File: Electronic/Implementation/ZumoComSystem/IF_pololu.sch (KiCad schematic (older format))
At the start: 38 parts, among them J4 Left, J5 Conn_02x07_Odd_Even, J6 Right, J7 Conn_02x07_Odd_Even, Q10 SI2302CDS-T1-BE3, Q6 SI2302CDS-T1-BE3, Q7 SI2302CDS-T1-BE3, Q8 SI2302CDS-T1-BE3, Q9 SI2302CDS-T1-BE3, SW3 SW_Push, SW4 SW_Push, SW5 SW_Push

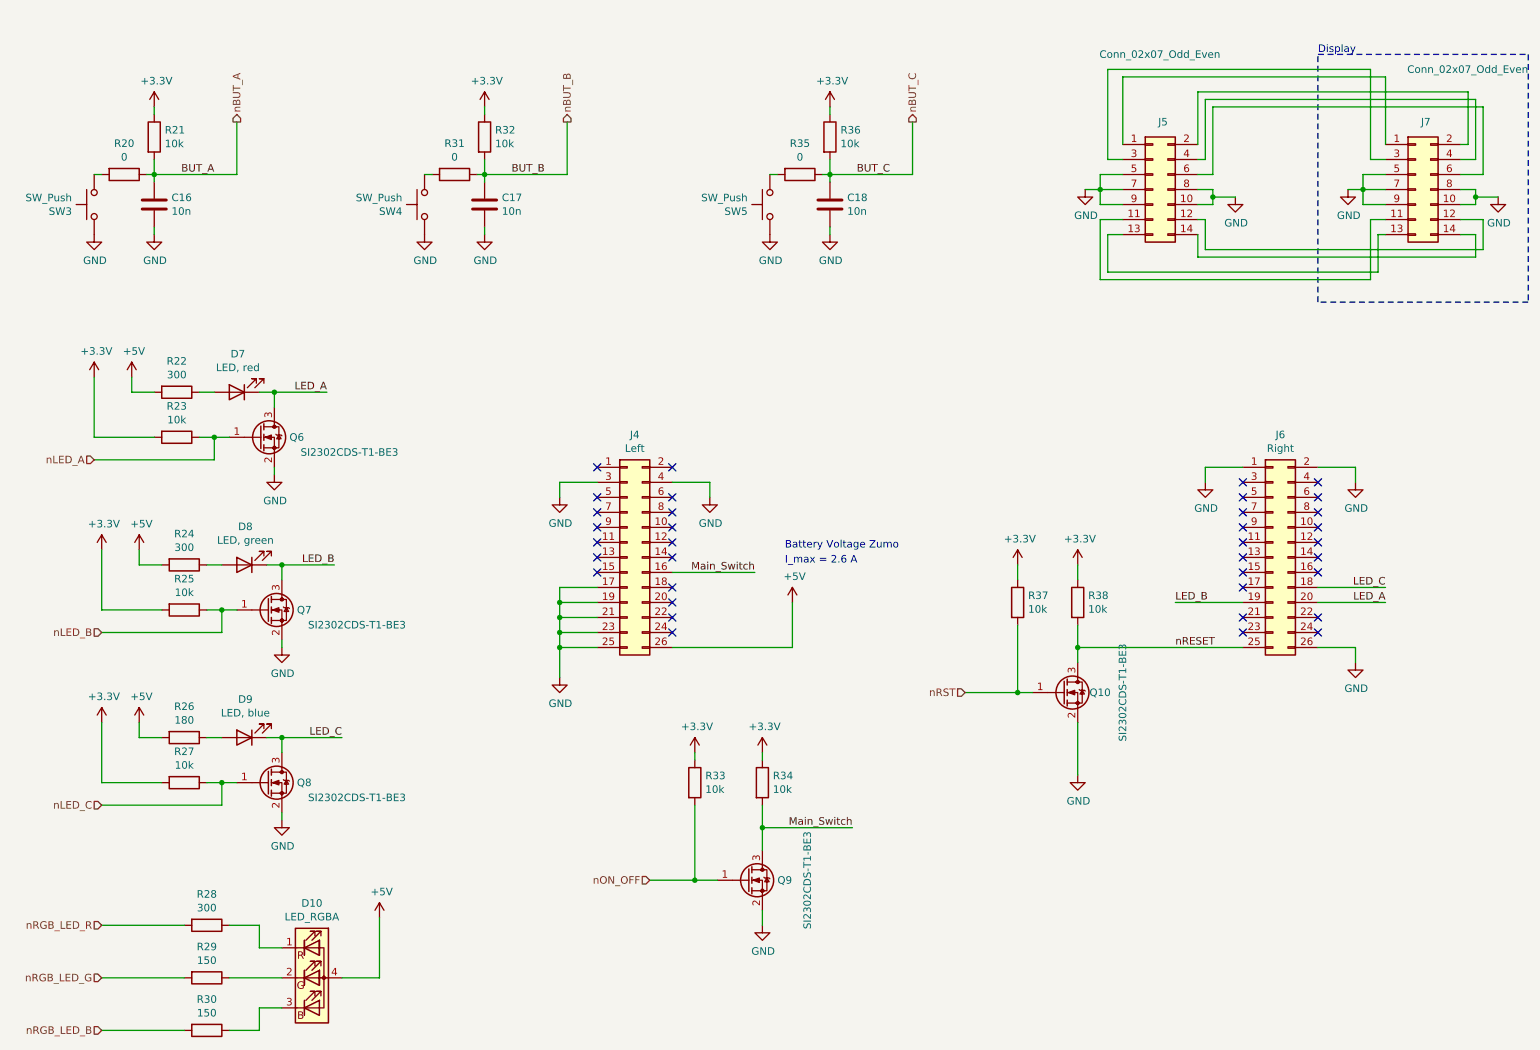
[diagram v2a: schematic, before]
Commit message: Electronic: ZumoCom System: finhished/ orderd PCB + add Version and TOP/BOT on PCB
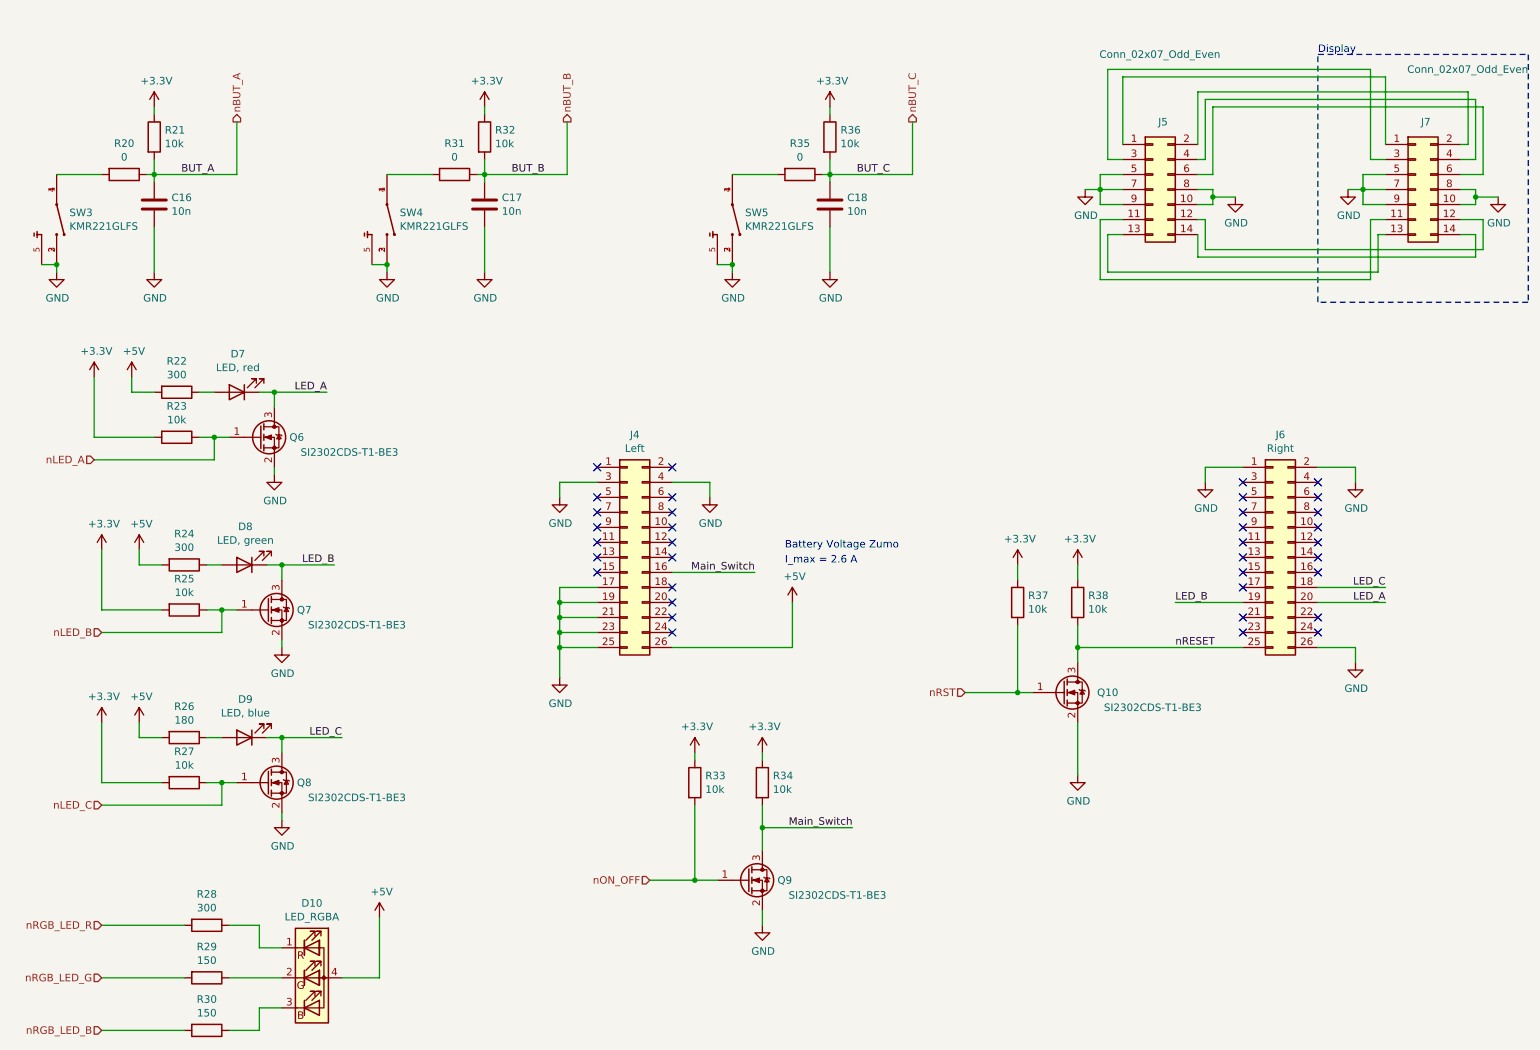
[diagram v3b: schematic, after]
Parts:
- removed SW3, SW4, SW5: SW_Push, Button_Switch_SMD:SW_SPST_B3U-1000P-B, symbol Switch:SW_Push
- added SW3, SW4, SW5: KMR221GLFS, footprints:SW_KMR221GLFS, symbol KMR221GLFS:KMR221GLFS
- R26: Part-No. RL73N1JR18JTD -> CRGP0603F180R
- R29, R30: Manufacturer Panasonic Electronic Components -> YAGEO; Part-No. ERJ-3RSFR15V -> RC0603FR-07150RL
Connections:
- net GND: now also SW3.2, SW3.3, SW3.5, SW4.2, SW4.3, SW4.5, SW5.2, SW5.3, SW5.5
- net at R31.2: now also SW4.1, SW4.4
- net at R35.2: now also SW5.1, SW5.4
- net at R20.2: now also SW3.1, SW3.4
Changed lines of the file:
@@
 Sheet 7 7
 Title "Zumo Communication System"
-Date "2022-04-22"
+Date "2022-05-13"
 Rev "V1.0"
 Comp "NewTec GmbH"
@@
 F 2 "Resistor_SMD:R_0603_1608Metric_Pad1.05x0.95mm_HandSolder" V 2030 6900 50  0001 C CNN
 F 3 "~" H 2100 6900 50  0001 C CNN
-F 4 "Panasonic Electronic Components" H 2100 6900 50  0001 C CNN "Manufacturer"
-F 5 "ERJ-3RSFR15V" H 2100 6900 50  0001 C CNN "Part-No."
+F 4 "YAGEO" H 2100 6900 50  0001 C CNN "Manufacturer"
+F 5 "RC0603FR-07150RL" H 2100 6900 50  0001 C CNN "Part-No."
 	1    2100 6900
 	0    1    1    0
@@
 F 2 "Resistor_SMD:R_0603_1608Metric_Pad1.05x0.95mm_HandSolder" V 2030 7250 50  0001 C CNN
 F 3 "~" H 2100 7250 50  0001 C CNN
-F 4 "Panasonic Electronic Components" H 2100 7250 50  0001 C CNN "Manufacturer"
-F 5 "ERJ-3RSFR15V" H 2100 7250 50  0001 C CNN "Part-No."
+F 4 "YAGEO" H 2100 7250 50  0001 C CNN "Manufacturer"
+F 5 "RC0603FR-07150RL" H 2100 7250 50  0001 C CNN "Part-No."
 	1    2100 7250
 	0    1    1    0
@@
 Wire Wire Line
 	3950 1450 3950 1550
-$Comp
-L Switch:SW_Push SW4
-U 1 1 61349AA0
-P 3550 1750
-F 0 "SW4" V 3504 1898 50  0000 L CNN
-F 1 "SW_Push" V 3595 1898 50  0000 L CNN
-F 2 "Button_Switch_SMD:SW_SPST_B3U-1000P-B" H 3550 1950 50  0001 C CNN
-F 3 "https://omronfs.omron.com/en_US/ecb/products/pdf/en-b3u.pdf" H 3550 1950 50  0001 C CNN
-F 4 " Omron Electronics" H 3550 1750 50  0001 C CNN "Manufacturer"
-F 5 "B3U-1000P-B" H 3550 1750 50  0001 C CNN "Part-No."
-	1    3550 1750
-	0    -1   -1   0
-$EndComp
-$Comp
-L power:GND #PWR057
-U 1 1 61349AA8
-P 3550 1950
-F 0 "#PWR057" H 3550 1700 50  0001 C CNN
-F 1 "GND" H 3555 1777 50  0000 C CNN
-F 2 "" H 3550 1950 50  0001 C CNN
-F 3 "" H 3550 1950 50  0001 C CNN
-	1    3550 1950
-	1    0    0    -1
-$EndComp
 $Comp
 L power:+3.3V #PWR068
@@
 $EndComp
 Wire Wire Line
-	3550 1550 3600 1550
+	3300 1550 3600 1550
 Wire Wire Line
 	3950 1550 3900 1550
 Connection ~ 6250 1550
-$Comp
-L Switch:SW_Push SW5
-U 1 1 617BFBA9
-P 5850 1750
-F 0 "SW5" V 5804 1898 50  0000 L CNN
-F 1 "SW_Push" V 5895 1898 50  0000 L CNN
-F 2 "Button_Switch_SMD:SW_SPST_B3U-1000P-B" H 5850 1950 50  0001 C CNN
-F 3 "https://omronfs.omron.com/en_US/ecb/products/pdf/en-b3u.pdf" H 5850 1950 50  0001 C CNN
-F 4 " Omron Electronics" H 5850 1750 50  0001 C CNN "Manufacturer"
-F 5 "B3U-1000P-B" H 5850 1750 50  0001 C CNN "Part-No."
-	1    5850 1750
-	0    -1   -1   0
-$EndComp
-$Comp
-L power:GND #PWR066
-U 1 1 617BFBAF
-P 5850 1950
-F 0 "#PWR066" H 5850 1700 50  0001 C CNN
-F 1 "GND" H 5855 1777 50  0000 C CNN
-F 2 "" H 5850 1950 50  0001 C CNN
-F 3 "" H 5850 1950 50  0001 C CNN
-	1    5850 1950
-	1    0    0    -1
-$EndComp
 $Comp
 L Device:R R35
@@
 $EndComp
 Wire Wire Line
-	5850 1550 5900 1550
+	5600 1550 5900 1550
 Wire Wire Line
 	6250 1550 6200 1550
-$Comp
-L Switch:SW_Push SW3
-U 1 1 617DBB37
-P 1350 1750
-F 0 "SW3" V 1304 1898 50  0000 L CNN
-F 1 "SW_Push" V 1395 1898 50  0000 L CNN
-F 2 "Button_Switch_SMD:SW_SPST_B3U-1000P-B" H 1350 1950 50  0001 C CNN
-F 3 "https://omronfs.omron.com/en_US/ecb/products/pdf/en-b3u.pdf" H 1350 1950 50  0001 C CNN
-F 4 " Omron Electronics" H 1350 1750 50  0001 C CNN "Manufacturer"
-F 5 "B3U-1000P-B" H 1350 1750 50  0001 C CNN "Part-No."
-	1    1350 1750
-	0    -1   -1   0
-$EndComp
 $Comp
 L power:GND #PWR044
 U 1 1 617DBB3D
-P 1350 1950
-F 0 "#PWR044" H 1350 1700 50  0001 C CNN
-F 1 "GND" H 1355 1777 50  0000 C CNN
-F 2 "" H 1350 1950 50  0001 C CNN
-F 3 "" H 1350 1950 50  0001 C CNN
-	1    1350 1950
+P 1100 2200
+F 0 "#PWR044" H 1100 1950 50  0001 C CNN
+F 1 "GND" H 1105 2027 50  0000 C CNN
+F 2 "" H 1100 2200 50  0001 C CNN
+F 3 "" H 1100 2200 50  0001 C CNN
+	1    1100 2200
 	1    0    0    -1
 $EndComp
@@
 	0    1    1    0
 $EndComp
-Wire Wire Line
-	1350 1550 1400 1550
 $Comp
 L power:GND #PWR055
@@
 F 3 "~" H 1950 5300 50  0001 C CNN
 F 4 "TE Connectivity Passive Product" H 1950 5300 50  0001 C CNN "Manufacturer"
-F 5 "RL73N1JR18JTD" H 1950 5300 50  0001 C CNN "Part-No."
+F 5 "CRGP0603F180R" H 1950 5300 50  0001 C CNN "Part-No."
 	1    1950 5300
 	0    1    1    0
@@
 AR Path="/60C50401/6232FCBD" Ref="Q9"  Part="1"
 F 0 "Q9" H 5949 6250 50  0000 C CNN
-F 1 "SI2302CDS-T1-BE3" V 6100 6250 50  0000 C CNN
+F 1 "SI2302CDS-T1-BE3" H 6300 6150 50  0000 C CNN
 F 2 "Package_TO_SOT_SMD:SOT-23" H 5900 6350 50  0001 C CNN
 F 3 "https://www.mouser.de/datasheet/2/196/Infineon_IRLML6246_DataSheet_v01_01_EN-1228486.pdf" H 5700 6250 50  0001 C CNN
@@
 F 5 "SI2302CDS-T1-BE3" H 5700 6250 50  0001 C CNN "Part-No."
 	1    5700 6250
-	1    0    0    -1
-$EndComp
-$Comp
-L Device:Q_NMOS_GSD Q?
-U 1 1 62330FDB
-P 7800 5000
-AR Path="/60C3F332/62330FDB" Ref="Q?"  Part="1"
-AR Path="/60C50401/62330FDB" Ref="Q10"  Part="1"
-F 0 "Q10" H 8049 5000 50  0000 C CNN
-F 1 "SI2302CDS-T1-BE3" V 8200 5000 50  0000 C CNN
-F 2 "Package_TO_SOT_SMD:SOT-23" H 8000 5100 50  0001 C CNN
-F 3 "https://www.mouser.de/datasheet/2/196/Infineon_IRLML6246_DataSheet_v01_01_EN-1228486.pdf" H 7800 5000 50  0001 C CNN
-F 4 "Vishay / Siliconix" H 7800 5000 50  0001 C CNN "Manufacturer"
-F 5 "SI2302CDS-T1-BE3" H 7800 5000 50  0001 C CNN "Part-No."
-	1    7800 5000
 	1    0    0    -1
 $EndComp
@@
 L power:GND #PWR052
 U 1 1 62612FD9
-P 1750 1950
-F 0 "#PWR052" H 1750 1700 50  0001 C CNN
-F 1 "GND" H 1755 1777 50  0000 C CNN
-F 2 "" H 1750 1950 50  0001 C CNN
-F 3 "" H 1750 1950 50  0001 C CNN
-	1    1750 1950
-	1    0    0    -1
-$EndComp
-Wire Wire Line
-	1750 1950 1750 1900
+P 1750 2200
+F 0 "#PWR052" H 1750 1950 50  0001 C CNN
+F 1 "GND" H 1755 2027 50  0000 C CNN
+F 2 "" H 1750 2200 50  0001 C CNN
+F 3 "" H 1750 2200 50  0001 C CNN
+	1    1750 2200
+	1    0    0    -1
+$EndComp
+Wire Wire Line
+	1750 2200 1750 1900
 Wire Wire Line
 	1750 1600 1750 1550
@@
 	1    0    0    -1
 $EndComp
-$Comp
-L power:GND #PWR059
-U 1 1 6262756F
-P 3950 1950
-F 0 "#PWR059" H 3950 1700 50  0001 C CNN
-F 1 "GND" H 3955 1777 50  0000 C CNN
-F 2 "" H 3950 1950 50  0001 C CNN
-F 3 "" H 3950 1950 50  0001 C CNN
-	1    3950 1950
-	1    0    0    -1
-$EndComp
-Wire Wire Line
-	3950 1950 3950 1900
 Wire Wire Line
 	3950 1600 3950 1550
@@
 	1    0    0    -1
 $EndComp
+Wire Wire Line
+	6250 1600 6250 1550
+$Comp
+L KMR221GLFS:KMR221GLFS SW3
+U 1 1 627F711A
+P 1100 1850
+F 0 "SW3" V 1054 1935 50  0000 L CNN
+F 1 "KMR221GLFS" V 1145 1935 50  0000 L CNN
+F 2 "footprints:SW_KMR221GLFS" H 1100 1850 50  0001 L BNN
+F 3 "-" H 1100 1850 50  0001 L BNN
+F 4 " C&K" H 1100 1850 50  0001 C CNN "Manufacturer"
+F 5 "KMR221GLFS" H 1100 1850 50  0001 C CNN "Part-No."
+	1    1100 1850
+	0    1    1    0
+$EndComp
+Wire Wire Line
+	1000 2150 1100 2150
+Wire Wire Line
+	1100 1550 1400 1550
+$Comp
+L power:GND #PWR057
+U 1 1 6284D0AC
+P 3300 2200
+F 0 "#PWR057" H 3300 1950 50  0001 C CNN
+F 1 "GND" H 3305 2027 50  0000 C CNN
+F 2 "" H 3300 2200 50  0001 C CNN
+F 3 "" H 3300 2200 50  0001 C CNN
+	1    3300 2200
+	1    0    0    -1
+$EndComp
+$Comp
+L power:GND #PWR059
+U 1 1 6284D0B2
+P 3950 2200
+F 0 "#PWR059" H 3950 1950 50  0001 C CNN
+F 1 "GND" H 3955 2027 50  0000 C CNN
+F 2 "" H 3950 2200 50  0001 C CNN
+F 3 "" H 3950 2200 50  0001 C CNN
+	1    3950 2200
+	1    0    0    -1
+$EndComp
+$Comp
+L KMR221GLFS:KMR221GLFS SW4
+U 1 1 6284D0B9
+P 3300 1850
+F 0 "SW4" V 3254 1935 50  0000 L CNN
+F 1 "KMR221GLFS" V 3345 1935 50  0000 L CNN
+F 2 "footprints:SW_KMR221GLFS" H 3300 1850 50  0001 L BNN
+F 3 "-" H 3300 1850 50  0001 L BNN
+F 4 " C&K" H 3300 1850 50  0001 C CNN "Manufacturer"
+F 5 "KMR221GLFS" H 3300 1850 50  0001 C CNN "Part-No."
+	1    3300 1850
+	0    1    1    0
+$EndComp
+Wire Wire Line
+	3200 2150 3300 2150
+Wire Wire Line
+	3950 1900 3950 2200
+Wire Wire Line
+	1100 2150 1100 2200
+Connection ~ 1100 2150
+Wire Wire Line
+	3300 2150 3300 2200
+Connection ~ 3300 2150
+$Comp
+L power:GND #PWR066
+U 1 1 628C1E66
+P 5600 2200
+F 0 "#PWR066" H 5600 1950 50  0001 C CNN
+F 1 "GND" H 5605 2027 50  0000 C CNN
+F 2 "" H 5600 2200 50  0001 C CNN
+F 3 "" H 5600 2200 50  0001 C CNN
+	1    5600 2200
+	1    0    0    -1
+$EndComp
 $Comp
 L power:GND #PWR069
-U 1 1 6263BD60
-P 6250 1950
-F 0 "#PWR069" H 6250 1700 50  0001 C CNN
-F 1 "GND" H 6255 1777 50  0000 C CNN
-F 2 "" H 6250 1950 50  0001 C CNN
-F 3 "" H 6250 1950 50  0001 C CNN
-	1    6250 1950
-	1    0    0    -1
-$EndComp
-Wire Wire Line
-	6250 1950 6250 1900
-Wire Wire Line
-	6250 1600 6250 1550
+U 1 1 628C1E6C
+P 6250 2200
+F 0 "#PWR069" H 6250 1950 50  0001 C CNN
+F 1 "GND" H 6255 2027 50  0000 C CNN
+F 2 "" H 6250 2200 50  0001 C CNN
+F 3 "" H 6250 2200 50  0001 C CNN
+	1    6250 2200
+	1    0    0    -1
+$EndComp
+Wire Wire Line
+	6250 2200 6250 1900
+$Comp
+L KMR221GLFS:KMR221GLFS SW5
+U 1 1 628C1E73
+P 5600 1850
+F 0 "SW5" V 5554 1935 50  0000 L CNN
+F 1 "KMR221GLFS" V 5645 1935 50  0000 L CNN
+F 2 "footprints:SW_KMR221GLFS" H 5600 1850 50  0001 L BNN
+F 3 "-" H 5600 1850 50  0001 L BNN
+F 4 " C&K" H 5600 1850 50  0001 C CNN "Manufacturer"
+F 5 "KMR221GLFS" H 5600 1850 50  0001 C CNN "Part-No."
+	1    5600 1850
+	0    1    1    0
+$EndComp
+Wire Wire Line
+	5500 2150 5600 2150
+Wire Wire Line
+	5600 2150 5600 2200
+Connection ~ 5600 2150
+$Comp
+L Device:Q_NMOS_GSD Q?
+U 1 1 62330FDB
+P 7800 5000
+AR Path="/60C3F332/62330FDB" Ref="Q?"  Part="1"
+AR Path="/60C50401/62330FDB" Ref="Q10"  Part="1"
+F 0 "Q10" H 8100 5000 50  0000 C CNN
+F 1 "SI2302CDS-T1-BE3" H 8400 4900 50  0000 C CNN
+F 2 "Package_TO_SOT_SMD:SOT-23" H 8000 5100 50  0001 C CNN
+F 3 "https://www.mouser.de/datasheet/2/196/Infineon_IRLML6246_DataSheet_v01_01_EN-1228486.pdf" H 7800 5000 50  0001 C CNN
+F 4 "Vishay / Siliconix" H 7800 5000 50  0001 C CNN "Manufacturer"
+F 5 "SI2302CDS-T1-BE3" H 7800 5000 50  0001 C CNN "Part-No."
+	1    7800 5000
+	1    0    0    -1
+$EndComp
 $EndSCHEMATC
